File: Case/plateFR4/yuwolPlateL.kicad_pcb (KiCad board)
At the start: 2 copper layers, 173.5 x 126 mm, 0 parts

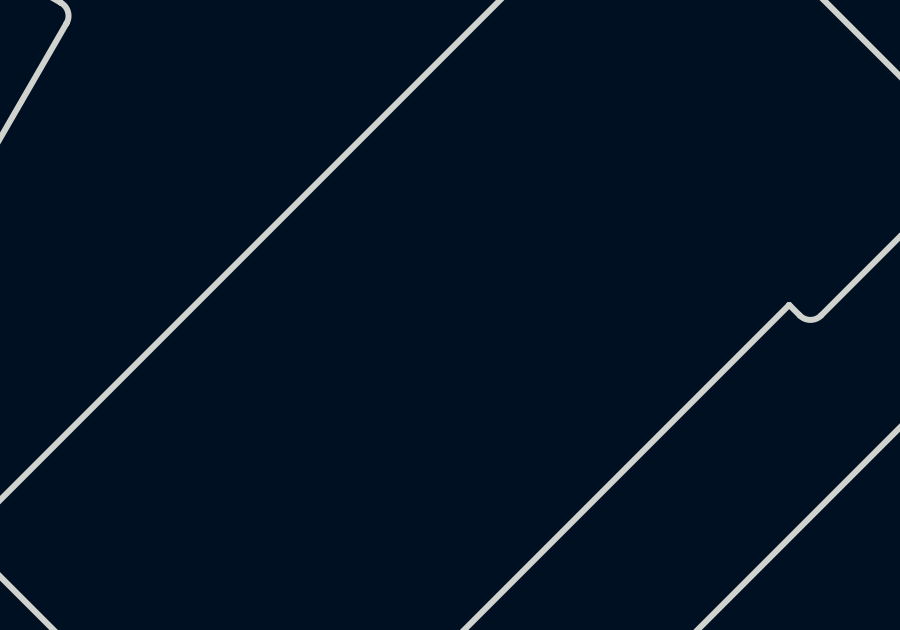
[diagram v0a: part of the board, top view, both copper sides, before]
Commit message: add tooling hole: because of drilling layer
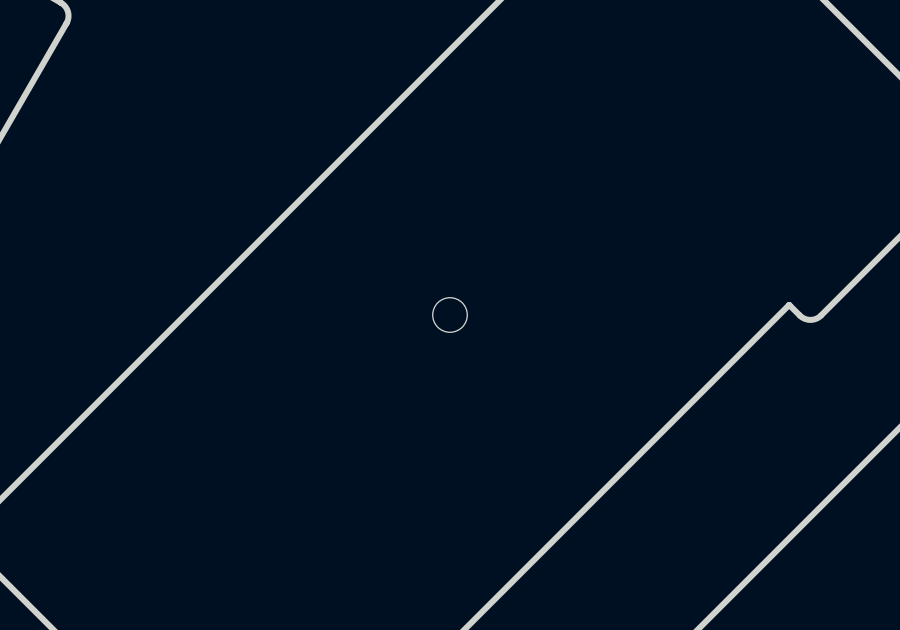
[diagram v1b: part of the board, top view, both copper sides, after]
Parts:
- added REF**: ToolingHole_1.152mm, MountingHole:ToolingHole_1.152mm, F.Cu at (207.0, 141.0)
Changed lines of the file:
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@@
 		)
+	)
+	(footprint "MountingHole:ToolingHole_1.152mm"
+		(layer "F.Cu")
+		(at 207 141)
+		(descr "Tooling Hole 1.152mm, 1.3mm solder mask, JLCPCB specification, https://jlcpcb.com/help/article/How-to-add-tooling-holes-for-PCB-assembly-order")
+		(tags "mounting")
+		(property "Reference" "REF**"
+			(at 0 -1.5 0)
+			(layer "F.SilkS")
+			(hide yes)
+			(effects
+				(font
+					(size 1 1)
+					(thickness 0.15)
+				)
+			)
+		)
+		(property "Value" "ToolingHole_1.152mm"
+			(at 0 1.6 0)
+			(layer "F.Fab")
+			(effects
+				(font
+					(size 1 1)
+					(thickness 0.15)
+				)
+			)
+		)
+		(property "Datasheet" ""
+			(at 0 0 0)
+			(unlocked yes)
+			(layer "F.Fab")
+			(hide yes)
+			(effects
+				(font
+					(size 1.27 1.27)
+					(thickness 0.15)
+				)
+			)
+		)
+		(property "Description" ""
+			(at 0 0 0)
+			(unlocked yes)
+			(layer "F.Fab")
+			(hide yes)
+			(effects
+				(font
+					(size 1.27 1.27)
+					(thickness 0.15)
+				)
+			)
+		)
+		(attr exclude_from_pos_files exclude_from_bom)
+		(duplicate_pad_numbers_are_jumpers no)
+		(fp_circle
+			(center 0 0)
+			(end 0.7 0)
+			(stroke
+				(width 0.05)
+				(type solid)
+			)
+			(fill no)
+			(layer "F.CrtYd")
+		)
+		(fp_text user "${REFERENCE}"
+			(at 0 0 0)
+			(layer "F.Fab")
+			(effects
+				(font
+					(size 1 1)
+					(thickness 0.15)
+				)
+			)
+		)
+		(pad "" np_thru_hole circle
+			(at 0 0)
+			(size 1.152 1.152)
+			(drill 1.152)
+			(layers "*.Cu" "*.Mask")
+			(solder_mask_margin 0.074)
+		)
+		(zone
+			(layers "F.Cu" "B.Cu")
+			(hatch edge 0.5)
+			(connect_pads
+				(clearance 0)
+			)
+			(min_thickness 0.25)
+			(keepout
+				(tracks not_allowed)
+				(vias allowed)
+				(pads allowed)
+				(copperpour not_allowed)
+				(footprints not_allowed)
+			)
+			(placement
+				(enabled no)
+				(sheetname "")
+			)
+			(fill
+				(thermal_gap 0.5)
+				(thermal_bridge_width 0.5)
+				(island_removal_mode 0)
+			)
+			(polygon
+				(pts
+					(xy 207.7 141) (xy 207.679659 140.832479) (xy 207.619819 140.674694) (xy 207.523958 140.535814)
+					(xy 207.397645 140.423911) (xy 207.248223 140.345489) (xy 207.084376 140.305104) (xy 206.915624 140.305104)
+					(xy 206.751777 140.345489) (xy 206.602355 140.423911) (xy 206.476042 140.535814) (xy 206.380181 140.674694)
+					(xy 206.320341 140.832479) (xy 206.3 141) (xy 206.320341 141.167521) (xy 206.380181 141.325306)
+					(xy 206.476042 141.464186) (xy 206.602355 141.576089) (xy 206.751777 141.654511) (xy 206.915624 141.694896)
+					(xy 207.084376 141.694896) (xy 207.248223 141.654511) (xy 207.397645 141.576089) (xy 207.523958 141.464186)
+					(xy 207.619819 141.325306) (xy 207.679659 141.167521)
+				)
+			)
+		)
+		(embedded_fonts no)
 	)
 	(gr_line
